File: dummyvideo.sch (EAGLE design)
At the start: 16 parts, among them IC1 NE555SO

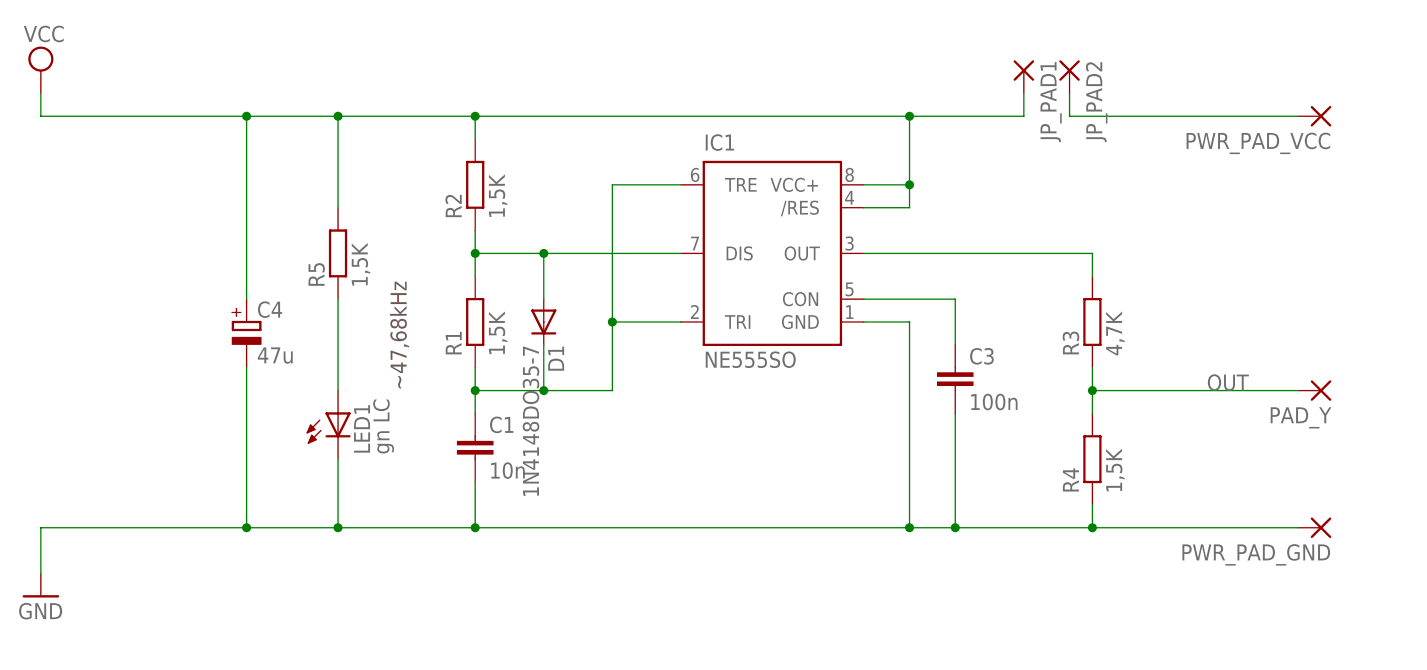
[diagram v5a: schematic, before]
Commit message: Changed layout to SMD variant.
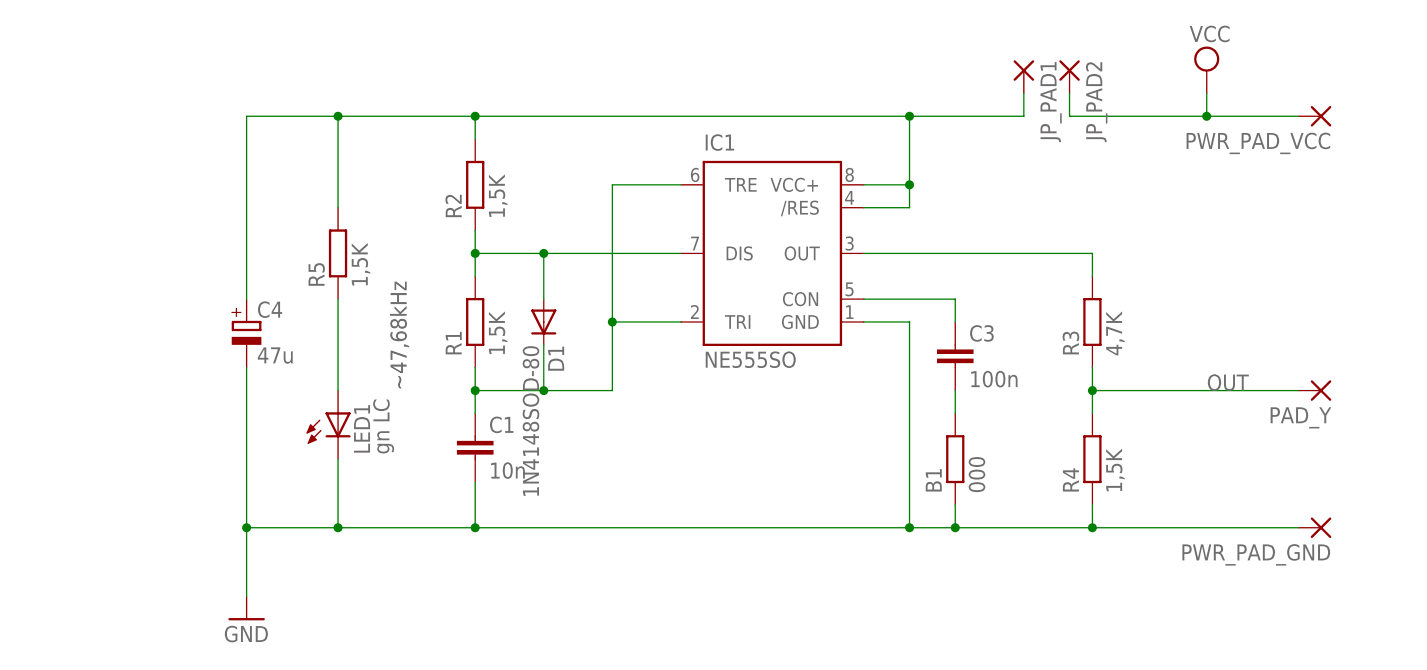
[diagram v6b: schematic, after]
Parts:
- added B1: 000, resistor:R-EU_R1206
- D1: value 1N4148DO35-7 -> 1N4148SOD-80; device diode:1N4148DO35-7 -> n39:1N4148SOD-80
- LED1: device led:LEDCHIPLED-0603-TTW -> led:LEDCHIP-LED0603
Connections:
- removed net N$6: JP_PAD2.P, PWR_PAD_VCC.P
- new net VCC_SW: C4.+, IC1./RES, IC1.VCC+, JP_PAD1.P, R2.2, R5.2
- net GND: now also B1.1, B1.2
- net VCC: now also JP_PAD2.P, PWR_PAD_VCC.P; no longer C4.+, IC1./RES, IC1.VCC+, JP_PAD1.P, R2.2, R5.2
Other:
- moved on the sheet: C3
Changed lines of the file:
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@@
 <part name="R2" library="resistor" deviceset="R-EU_" device="M0805" value="1,5K"/>
 <part name="C1" library="resistor" deviceset="C-EU" device="C0805" value="10n"/>
-<part name="D1" library="diode" deviceset="1N4148" device="DO35-7"/>
+<part name="D1" library="n39" deviceset="1N4148" device="SOD-80" value="1N4148SOD-80"/>
 <part name="R3" library="resistor" deviceset="R-EU_" device="R0805" value="4,7K"/>
 <part name="R4" library="resistor" deviceset="R-EU_" device="R0805" value="1,5K"/>
-<part name="LED1" library="led" deviceset="LED" device="CHIPLED-0603-TTW" value="gn LC"/>
+<part name="LED1" library="led" deviceset="LED" device="CHIP-LED0603" value="gn LC"/>
 <part name="R5" library="resistor" deviceset="R-EU_" device="R0805" value="1,5K"/>
 <part name="JP_PAD1" library="wirepad" deviceset="SMD2" device=""/>
@@
 <part name="PWR_PAD_GND" library="wirepad" deviceset="SMD2" device=""/>
 <part name="PAD_Y" library="wirepad" deviceset="SMD2" device=""/>
+<part name="B1" library="resistor" deviceset="R-EU_" device="R1206" value="000"/>
 </parts>
 <sheets>
@@
 <instances>
 <instance part="IC1" gate="G$1" x="55.88" y="58.42"/>
-<instance part="GND1" gate="1" x="-25.4" y="20.32"/>
-<instance part="SUPPLY1" gate="G$1" x="-25.4" y="78.74"/>
+<instance part="GND1" gate="1" x="-2.54" y="17.78"/>
+<instance part="SUPPLY1" gate="G$1" x="104.14" y="78.74"/>
 <instance part="C4" gate="G$1" x="-2.54" y="50.8"/>
-<instance part="C3" gate="G$1" x="76.2" y="45.72"/>
+<instance part="C3" gate="G$1" x="76.2" y="48.26"/>
 <instance part="R1" gate="G$1" x="22.86" y="50.8" rot="R90"/>
 <instance part="R2" gate="G$1" x="22.86" y="66.04" rot="R90"/>
@@
 <instance part="PWR_PAD_GND" gate="1" x="116.84" y="27.94" rot="R180"/>
 <instance part="PAD_Y" gate="1" x="116.84" y="43.18" rot="R180"/>
+<instance part="B1" gate="G$1" x="76.2" y="35.56" rot="R90"/>
 </instances>
 <busses>
 </busses>
 <nets>
-<net name="VCC" class="0">
-<segment>
-<pinref part="IC1" gate="G$1" pin="VCC+"/>
-<wire x1="71.12" y1="73.66" x2="71.12" y2="66.04" width="0.1524" layer="91"/>
-<wire x1="71.12" y1="66.04" x2="66.04" y2="66.04" width="0.1524" layer="91"/>
-<pinref part="IC1" gate="G$1" pin="/RES"/>
-<wire x1="66.04" y1="63.5" x2="71.12" y2="63.5" width="0.1524" layer="91"/>
-<wire x1="71.12" y1="63.5" x2="71.12" y2="66.04" width="0.1524" layer="91"/>
-<junction x="71.12" y="66.04"/>
-<pinref part="R2" gate="G$1" pin="2"/>
-<wire x1="22.86" y1="71.12" x2="22.86" y2="73.66" width="0.1524" layer="91"/>
-<wire x1="22.86" y1="73.66" x2="71.12" y2="73.66" width="0.1524" layer="91"/>
-<wire x1="22.86" y1="73.66" x2="7.62" y2="73.66" width="0.1524" layer="91"/>
-<junction x="22.86" y="73.66"/>
-<pinref part="SUPPLY1" gate="G$1" pin="VCC"/>
-<wire x1="7.62" y1="73.66" x2="-2.54" y2="73.66" width="0.1524" layer="91"/>
-<wire x1="-2.54" y1="73.66" x2="-25.4" y2="73.66" width="0.1524" layer="91"/>
-<wire x1="-25.4" y1="73.66" x2="-25.4" y2="76.2" width="0.1524" layer="91"/>
-<pinref part="C4" gate="G$1" pin="+"/>
-<wire x1="-2.54" y1="53.34" x2="-2.54" y2="73.66" width="0.1524" layer="91"/>
-<junction x="-2.54" y="73.66"/>
-<pinref part="R5" gate="G$1" pin="2"/>
-<wire x1="7.62" y1="63.5" x2="7.62" y2="73.66" width="0.1524" layer="91"/>
-<junction x="7.62" y="73.66"/>
-<wire x1="71.12" y1="73.66" x2="83.82" y2="73.66" width="0.1524" layer="91"/>
-<junction x="71.12" y="73.66"/>
-<pinref part="JP_PAD1" gate="1" pin="P"/>
-<wire x1="83.82" y1="73.66" x2="83.82" y2="76.2" width="0.1524" layer="91"/>
-</segment>
-</net>
 <net name="GND" class="0">
 <segment>
@@
 <pinref part="GND1" gate="1" pin="GND"/>
 <wire x1="7.62" y1="27.94" x2="-2.54" y2="27.94" width="0.1524" layer="91"/>
-<wire x1="-2.54" y1="27.94" x2="-25.4" y2="27.94" width="0.1524" layer="91"/>
-<wire x1="-25.4" y1="27.94" x2="-25.4" y2="22.86" width="0.1524" layer="91"/>
+<wire x1="-2.54" y1="27.94" x2="-2.54" y2="20.32" width="0.1524" layer="91"/>
 <pinref part="C4" gate="G$1" pin="-"/>
 <wire x1="-2.54" y1="45.72" x2="-2.54" y2="27.94" width="0.1524" layer="91"/>
 <junction x="-2.54" y="27.94"/>
-<pinref part="C3" gate="G$1" pin="2"/>
-<wire x1="76.2" y1="40.64" x2="76.2" y2="27.94" width="0.1524" layer="91"/>
-<junction x="76.2" y="27.94"/>
+<wire x1="114.3" y1="27.94" x2="91.44" y2="27.94" width="0.1524" layer="91"/>
+<junction x="91.44" y="27.94"/>
+<pinref part="PWR_PAD_GND" gate="1" pin="P"/>
 <pinref part="LED1" gate="G$1" pin="C"/>
 <wire x1="7.62" y1="35.56" x2="7.62" y2="27.94" width="0.1524" layer="91"/>
 <junction x="7.62" y="27.94"/>
-<wire x1="114.3" y1="27.94" x2="91.44" y2="27.94" width="0.1524" layer="91"/>
-<junction x="91.44" y="27.94"/>
-<pinref part="PWR_PAD_GND" gate="1" pin="P"/>
+<pinref part="B1" gate="G$1" pin="1"/>
+<wire x1="76.2" y1="30.48" x2="76.2" y2="27.94" width="0.1524" layer="91"/>
+<junction x="76.2" y="27.94"/>
+</segment>
+<segment>
+<pinref part="C3" gate="G$1" pin="2"/>
+<pinref part="B1" gate="G$1" pin="2"/>
+<wire x1="76.2" y1="43.18" x2="76.2" y2="40.64" width="0.1524" layer="91"/>
 </segment>
 </net>
@@
 <wire x1="66.04" y1="53.34" x2="76.2" y2="53.34" width="0.1524" layer="91"/>
 <pinref part="C3" gate="G$1" pin="1"/>
-<wire x1="76.2" y1="53.34" x2="76.2" y2="48.26" width="0.1524" layer="91"/>
+<wire x1="76.2" y1="53.34" x2="76.2" y2="50.8" width="0.1524" layer="91"/>
 </segment>
 </net>
@@
 </segment>
 </net>
-<net name="N$6" class="0">
+<net name="VCC_SW" class="0">
+<segment>
+<pinref part="IC1" gate="G$1" pin="VCC+"/>
+<wire x1="71.12" y1="73.66" x2="71.12" y2="66.04" width="0.1524" layer="91"/>
+<wire x1="71.12" y1="66.04" x2="66.04" y2="66.04" width="0.1524" layer="91"/>
+<pinref part="IC1" gate="G$1" pin="/RES"/>
+<wire x1="66.04" y1="63.5" x2="71.12" y2="63.5" width="0.1524" layer="91"/>
+<wire x1="71.12" y1="63.5" x2="71.12" y2="66.04" width="0.1524" layer="91"/>
+<junction x="71.12" y="66.04"/>
+<pinref part="R2" gate="G$1" pin="2"/>
+<wire x1="22.86" y1="71.12" x2="22.86" y2="73.66" width="0.1524" layer="91"/>
+<wire x1="22.86" y1="73.66" x2="71.12" y2="73.66" width="0.1524" layer="91"/>
+<wire x1="22.86" y1="73.66" x2="7.62" y2="73.66" width="0.1524" layer="91"/>
+<junction x="22.86" y="73.66"/>
+<wire x1="7.62" y1="73.66" x2="-2.54" y2="73.66" width="0.1524" layer="91"/>
+<pinref part="C4" gate="G$1" pin="+"/>
+<wire x1="-2.54" y1="53.34" x2="-2.54" y2="73.66" width="0.1524" layer="91"/>
+<pinref part="R5" gate="G$1" pin="2"/>
+<wire x1="7.62" y1="63.5" x2="7.62" y2="73.66" width="0.1524" layer="91"/>
+<junction x="7.62" y="73.66"/>
+<wire x1="71.12" y1="73.66" x2="83.82" y2="73.66" width="0.1524" layer="91"/>
+<junction x="71.12" y="73.66"/>
+<pinref part="JP_PAD1" gate="1" pin="P"/>
+<wire x1="83.82" y1="73.66" x2="83.82" y2="76.2" width="0.1524" layer="91"/>
+</segment>
+</net>
+<net name="VCC" class="0">
 <segment>
 <pinref part="JP_PAD2" gate="1" pin="P"/>
 <wire x1="88.9" y1="76.2" x2="88.9" y2="73.66" width="0.1524" layer="91"/>
-<wire x1="88.9" y1="73.66" x2="114.3" y2="73.66" width="0.1524" layer="91"/>
+<wire x1="88.9" y1="73.66" x2="104.14" y2="73.66" width="0.1524" layer="91"/>
 <pinref part="PWR_PAD_VCC" gate="1" pin="P"/>
+<pinref part="SUPPLY1" gate="G$1" pin="VCC"/>
+<wire x1="104.14" y1="73.66" x2="114.3" y2="73.66" width="0.1524" layer="91"/>
+<wire x1="104.14" y1="76.2" x2="104.14" y2="73.66" width="0.1524" layer="91"/>
+<junction x="104.14" y="73.66"/>
 </segment>
 </net>

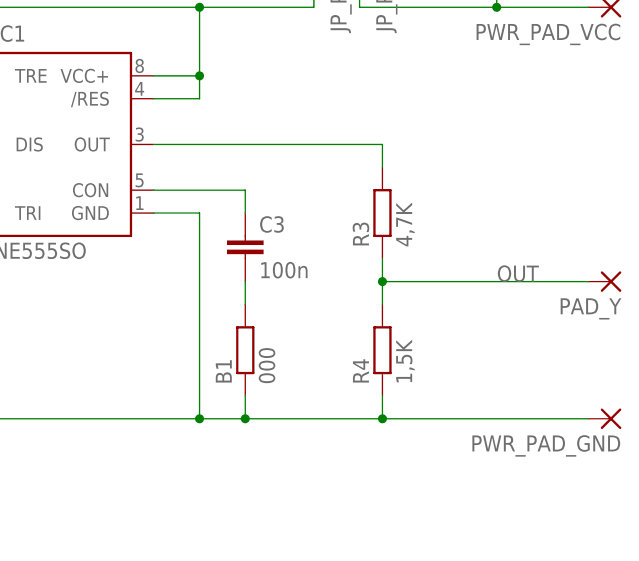
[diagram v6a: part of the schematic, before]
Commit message: Spannungsteiler war zu hochohmig -> angepasst
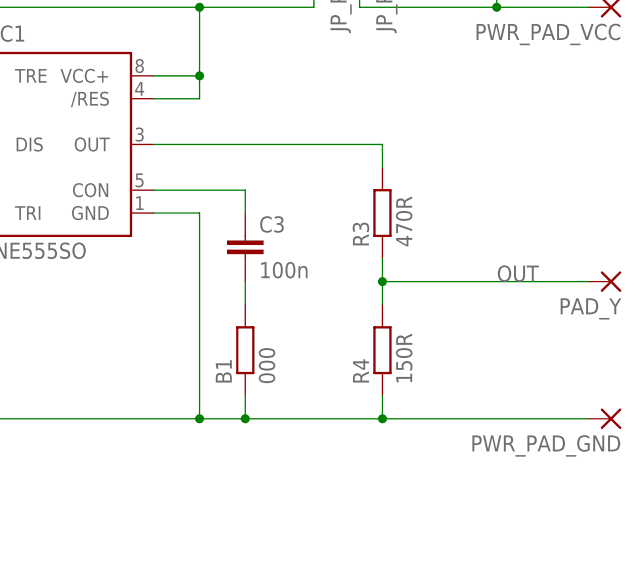
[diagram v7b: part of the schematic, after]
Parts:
- R3: value 4,7K -> 470R
- R4: value 1,5K -> 150R
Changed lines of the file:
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@@
 <grid distance="0.1" unitdist="inch" unit="inch" style="lines" multiple="1" display="no" altdistance="0.01" altunitdist="inch" altunit="inch"/>
 <layers>
-<layer number="1" name="Top" color="4" fill="1" visible="yes" active="no"/>
-<layer number="16" name="Bottom" color="1" fill="1" visible="yes" active="no"/>
-<layer number="17" name="Pads" color="2" fill="1" visible="yes" active="no"/>
-<layer number="18" name="Vias" color="2" fill="1" visible="yes" active="no"/>
-<layer number="19" name="Unrouted" color="6" fill="1" visible="yes" active="no"/>
-<layer number="20" name="Dimension" color="15" fill="1" visible="yes" active="no"/>
-<layer number="21" name="tPlace" color="7" fill="1" visible="yes" active="no"/>
-<layer number="22" name="bPlace" color="7" fill="1" visible="yes" active="no"/>
-<layer number="23" name="tOrigins" color="15" fill="1" visible="yes" active="no"/>
-<layer number="24" name="bOrigins" color="15" fill="1" visible="yes" active="no"/>
-<layer number="25" name="tNames" color="7" fill="1" visible="yes" active="no"/>
-<layer number="26" name="bNames" color="7" fill="1" visible="yes" active="no"/>
-<layer number="27" name="tValues" color="7" fill="1" visible="yes" active="no"/>
-<layer number="28" name="bValues" color="7" fill="1" visible="yes" active="no"/>
+<layer number="1" name="Top" color="4" fill="1" visible="no" active="no"/>
+<layer number="16" name="Bottom" color="1" fill="1" visible="no" active="no"/>
+<layer number="17" name="Pads" color="2" fill="1" visible="no" active="no"/>
+<layer number="18" name="Vias" color="2" fill="1" visible="no" active="no"/>
+<layer number="19" name="Unrouted" color="6" fill="1" visible="no" active="no"/>
+<layer number="20" name="Dimension" color="15" fill="1" visible="no" active="no"/>
+<layer number="21" name="tPlace" color="7" fill="1" visible="no" active="no"/>
+<layer number="22" name="bPlace" color="7" fill="1" visible="no" active="no"/>
+<layer number="23" name="tOrigins" color="15" fill="1" visible="no" active="no"/>
+<layer number="24" name="bOrigins" color="15" fill="1" visible="no" active="no"/>
+<layer number="25" name="tNames" color="7" fill="1" visible="no" active="no"/>
+<layer number="26" name="bNames" color="7" fill="1" visible="no" active="no"/>
+<layer number="27" name="tValues" color="7" fill="1" visible="no" active="no"/>
+<layer number="28" name="bValues" color="7" fill="1" visible="no" active="no"/>
 <layer number="29" name="tStop" color="7" fill="3" visible="no" active="no"/>
 <layer number="30" name="bStop" color="7" fill="6" visible="no" active="no"/>
@@
 <layer number="35" name="tGlue" color="7" fill="4" visible="no" active="no"/>
 <layer number="36" name="bGlue" color="7" fill="5" visible="no" active="no"/>
-<layer number="37" name="tTest" color="7" fill="1" visible="yes" active="no"/>
-<layer number="38" name="bTest" color="7" fill="1" visible="yes" active="no"/>
+<layer number="37" name="tTest" color="7" fill="1" visible="no" active="no"/>
+<layer number="38" name="bTest" color="7" fill="1" visible="no" active="no"/>
 <layer number="39" name="tKeepout" color="4" fill="11" visible="no" active="no"/>
 <layer number="40" name="bKeepout" color="1" fill="11" visible="no" active="no"/>
@@
 <layer number="44" name="Drills" color="7" fill="1" visible="no" active="no"/>
 <layer number="45" name="Holes" color="7" fill="1" visible="no" active="no"/>
-<layer number="46" name="Milling" color="3" fill="1" visible="yes" active="no"/>
-<layer number="47" name="Measures" color="7" fill="1" visible="yes" active="no"/>
-<layer number="48" name="Document" color="7" fill="1" visible="yes" active="no"/>
-<layer number="49" name="Reference" color="7" fill="1" visible="yes" active="no"/>
-<layer number="51" name="tDocu" color="7" fill="1" visible="yes" active="no"/>
-<layer number="52" name="bDocu" color="7" fill="1" visible="yes" active="no"/>
+<layer number="46" name="Milling" color="3" fill="1" visible="no" active="no"/>
+<layer number="47" name="Measures" color="7" fill="1" visible="no" active="no"/>
+<layer number="48" name="Document" color="7" fill="1" visible="no" active="no"/>
+<layer number="49" name="Reference" color="7" fill="1" visible="no" active="no"/>
+<layer number="51" name="tDocu" color="7" fill="1" visible="no" active="no"/>
+<layer number="52" name="bDocu" color="7" fill="1" visible="no" active="no"/>
 <layer number="91" name="Nets" color="2" fill="1" visible="yes" active="yes"/>
 <layer number="92" name="Busses" color="1" fill="1" visible="yes" active="yes"/>
@@
 <part name="C1" library="resistor" deviceset="C-EU" device="C0805" value="10n"/>
 <part name="D1" library="n39" deviceset="1N4148" device="SOD-80" value="1N4148SOD-80"/>
-<part name="R3" library="resistor" deviceset="R-EU_" device="R0805" value="4,7K"/>
-<part name="R4" library="resistor" deviceset="R-EU_" device="R0805" value="1,5K"/>
+<part name="R3" library="resistor" deviceset="R-EU_" device="R0805" value="470R"/>
+<part name="R4" library="resistor" deviceset="R-EU_" device="R0805" value="150R"/>
 <part name="LED1" library="led" deviceset="LED" device="CHIP-LED0603" value="gn LC"/>
 <part name="R5" library="resistor" deviceset="R-EU_" device="R0805" value="1,5K"/>
